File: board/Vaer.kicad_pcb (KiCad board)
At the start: 2 copper layers, 90 x 65 mm, 42 parts, among them J1 Conn_01x03_Pin, J2 Conn_01x03_Pin, J3 Conn_01x04_Pin, J4 GSB1C211110DS1HR, U1 BME280, U2 ESP32-S3-WROOM-1, U3 NCP1117-3.3_SOT223, U4 BQ24073RGT, U5 USB6B1

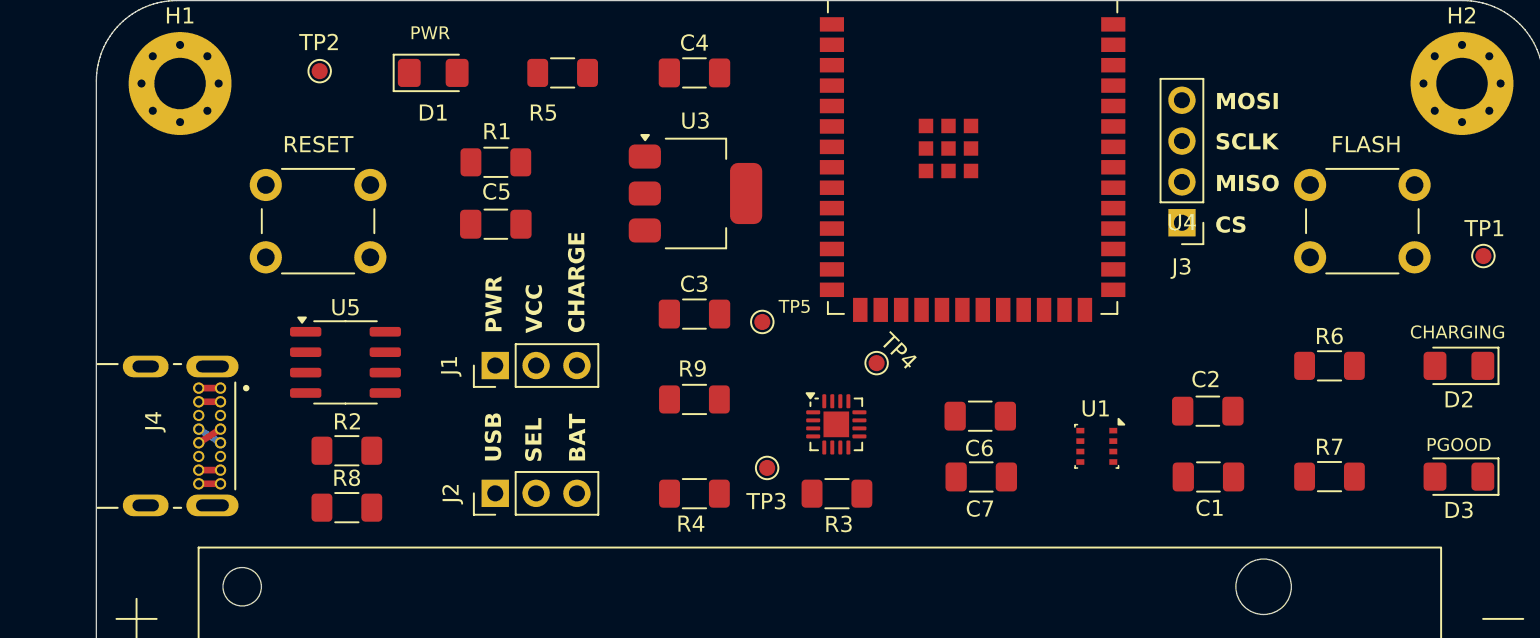
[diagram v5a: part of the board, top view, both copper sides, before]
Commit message: :recycle: Replace the Amphenol USB-C port by Molex USB-C port
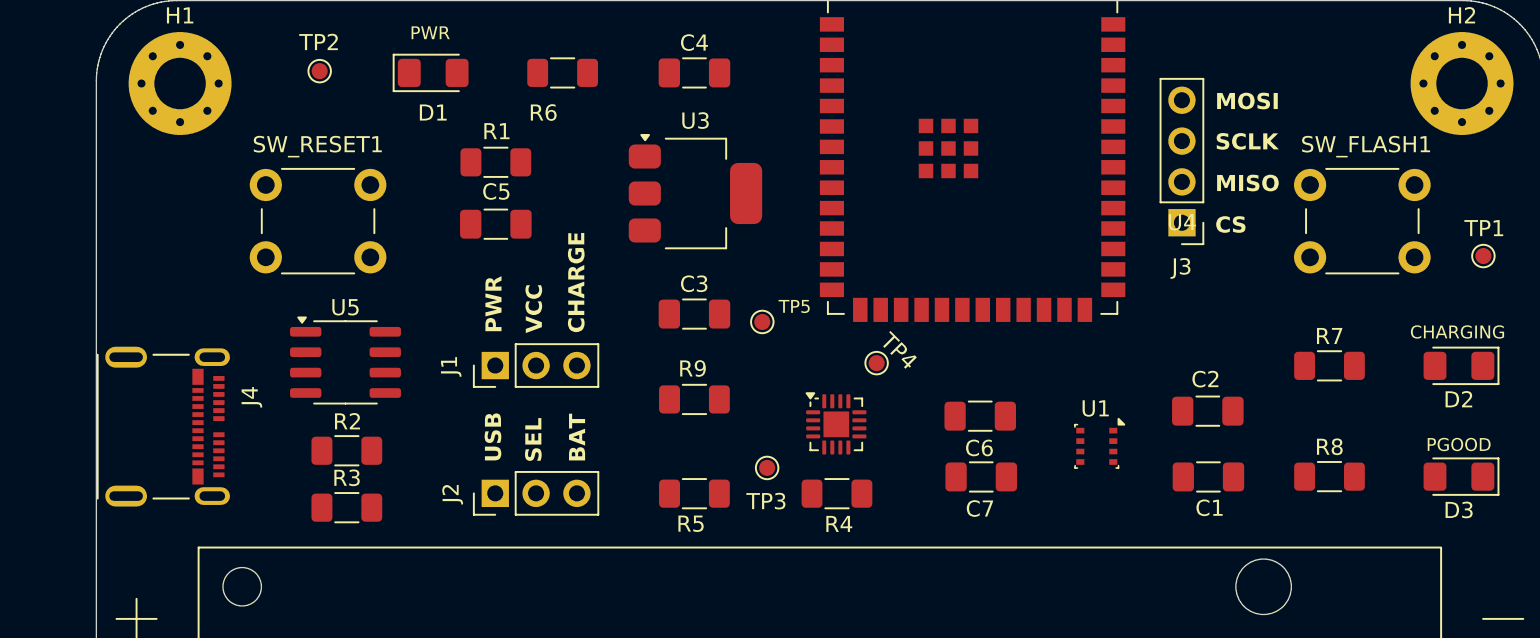
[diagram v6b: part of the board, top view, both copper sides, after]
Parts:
- J4: value GSB1C211110DS1HR -> 105450-0101; footprint USB-C:AMPHENOL_GSB1C211110DS1HR -> USB-C:MOLEX_105450-0101
- moved J4 0.61 mm to (88.8, 89.0)
- renumbered R8 to R3, R3 to R4, R4 to R5, R5 to R6, R6 to R7, R7 to R8, FLASH to SW_FLASH1, RESET to SW_RESET1
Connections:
- R3 pad 1: Net-(J4-CC2) -> GND
- R3 pad 2: GND -> Net-(J4-CC2)

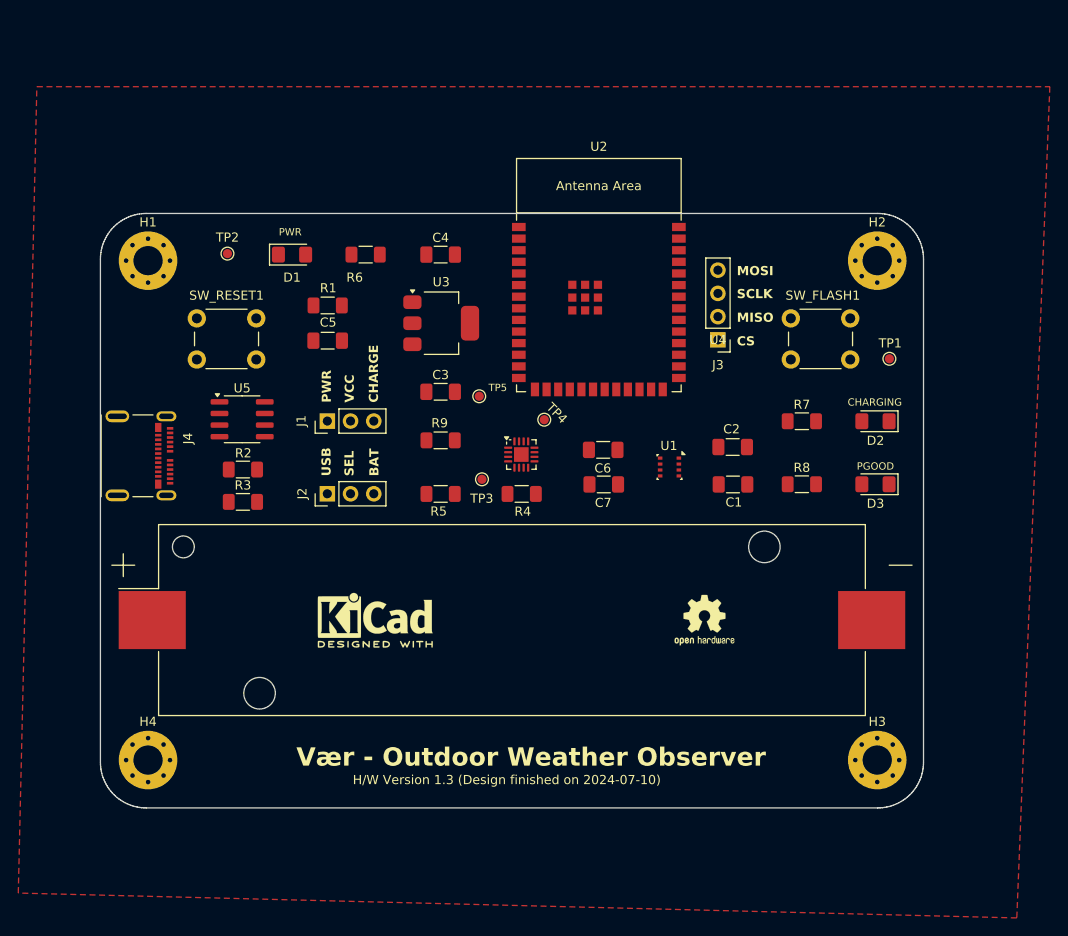
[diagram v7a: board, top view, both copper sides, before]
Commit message: :sparkles: Re-connect all components
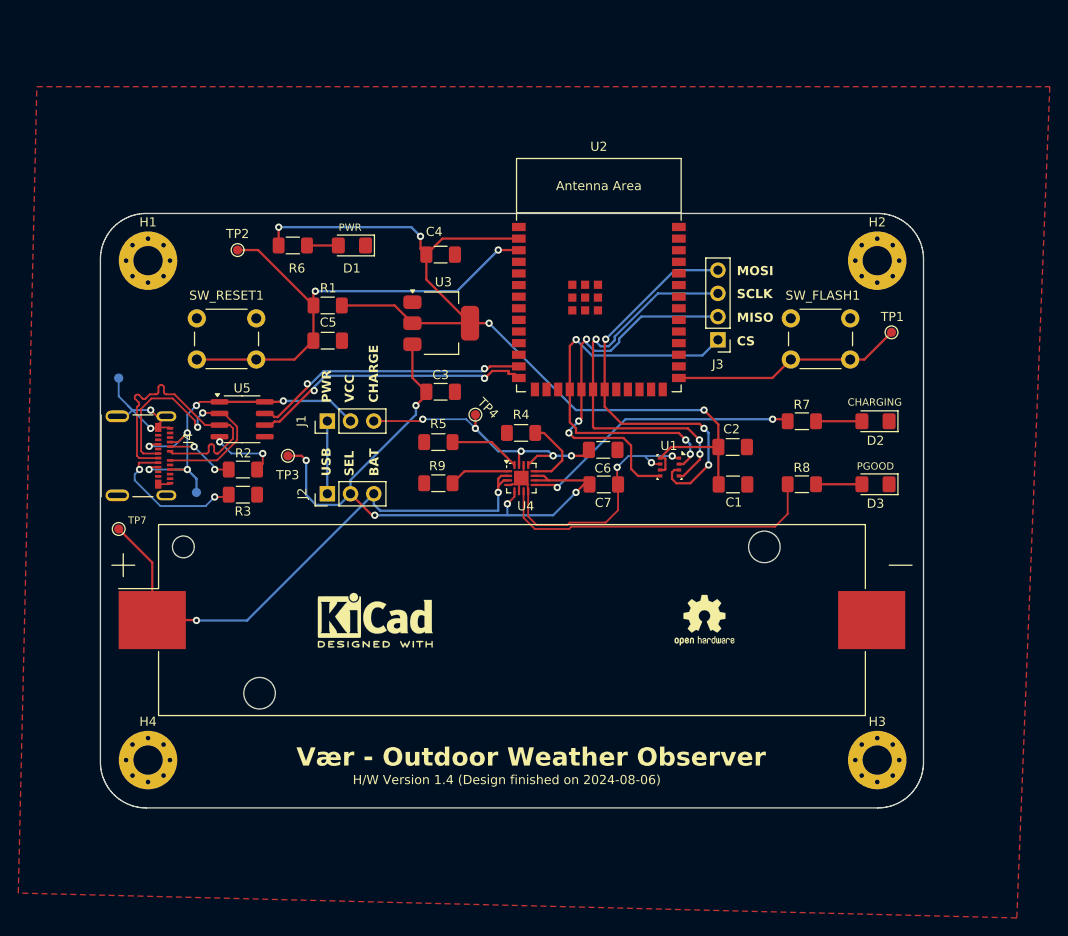
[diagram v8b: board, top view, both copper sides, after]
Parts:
- added TP5: TestPoint, TestPoint:TestPoint_Pad_D1.0mm, B.Cu at (87.0, 80.5)
- added TP6: TestPoint, TestPoint:TestPoint_Pad_D1.0mm, B.Cu at (95.5, 93.0)
- moved TP7 42.0 mm to (87.0, 97.0)
- moved TP3 21.4 mm to (105.5, 89.0)
- moved R6 8.03 mm to (106.0, 66.0), turned to 0 degrees
- moved TP4 7.55 mm to (126.0, 84.5)
- moved R4 6.67 mm to (131.0, 86.5)
- moved D1 6.63 mm to (112.5, 66.0), turned to 180 degrees
- moved R5 5.68 mm to (122.0, 87.5)
- moved R9 4.70 mm to (122.0, 92.0)
- moved TP1 2.90 mm to (171.5, 75.5)
- moved U4 2.58 mm to (131.0, 91.4)
- moved TP2 1.18 mm to (100.0, 66.5)
- moved R3 0.79 mm to (100.6, 93.2), turned to 180 degrees
- renumbered TP5 to TP7
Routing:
- net VCC_3V3: track 0.00 -> 102.9 mm, vias 0 -> 4
- net VCC_SEL: track 0.00 -> 71.6 mm, vias 0 -> 5
- net VCC_BAT: track 0.00 -> 62.5 mm, vias 0 -> 2
- net GND: track 0.00 -> 60.9 mm, vias 0 -> 7
- net EN: track 0.00 -> 54.0 mm, vias 0 -> 2
- net MOSI: track 0.00 -> 45.5 mm, vias 0 -> 3
- net CS: track 0.00 -> 43.7 mm, vias 0 -> 3
- net SCLK: track 0.00 -> 43.6 mm, vias 0 -> 3
- net VCC_USB: track 0.00 -> 43.6 mm, vias 0 -> 6
- net MISO: track 0.00 -> 41.4 mm, vias 0 -> 3
- net ~{PGOOD}: track 0.00 -> 36.4 mm
- net D_{internal}+: track 0.00 -> 33.8 mm
- net VCC_USB_CHARGE: track 0.00 -> 31.8 mm, vias 0 -> 5
- net D+: track 0.00 -> 31.2 mm, vias 0 -> 2
- net ~{CHG}: track 0.00 -> 31.0 mm, vias 0 -> 2
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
